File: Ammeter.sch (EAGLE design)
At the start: 81 parts, among them IC1 TL081P, IC2 TL081P, IC3 ICL7107, IC4 TL081P, IC5 TL081P, IC6 TL081P, IC7 TL081P, IC8 TL081P, IC9 TL081P, T1 BD139

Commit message: fixed errors in schematic and added BOM
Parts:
- added D4: BZX85C5V6, diode:BZX85
- added R55: 500, rcl:POTENTIOMETER_PT_SPIN
- D1, D2: value BZV10 -> BZX85C5V1; device diode:BZV10 -> diode:BZX85
- D3: value BZV10 -> BAT42; device diode:BZV10 -> diode:BAT42; SPICEPREFIX D -> (none)
- R14: value 82k -> 270
- R15: value 20k -> 270
- R17: value 270 -> 100k; device resistor:R-EU_0204/7 -> rcl:POTENTIOMETER_PT_SPIN
- R18: value 270 -> 20k
- R19: value 1M -> 100k
- R2: value 43k -> 270
- R20: value 100k -> 470k
- R21: value 470k -> 270
- R23, R9: value 270 -> 1M
- R29: value 110 -> 270
- R3: value 4k7 -> 100
- R31: value 270 -> 110
- R4: value 270 -> 50k; device resistor:R-EU_0204/7 -> rcl:POTENTIOMETER_PT_SPIN
- R46, R47: value 100k -> 15K
- R5: value 100 -> 4k7
- R50: value 16k -> 5k; device resistor:R-EU_0204/7 -> rcl:POTENTIOMETER_PT_SPIN
- R51: value (none) -> 16k; device rcl:POTENTIOMETER_PT_SPIN -> resistor:R-EU_0204/7
- R52: value 2k -> 20k; device resistor:R-EU_0204/7 -> rcl:POTENTIOMETER_PT_SPIN
- R53: value 2k -> 300
- R54: value (none) -> 2k
- R8: value 1M -> 270
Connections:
- net N$27 renamed 4-20
- removed net ICL_BP: IC3.BP, R23.1
- removed net V_REF: IC3.REF-HI
- new net N$5: DIS3.DP, R10.2
- new net N$52: IC8.OUT, R52.2
- net +12V: now also D3.C, R31.2; no longer G1.-, G2.+, R29.2
- net +5V: now also D4.C, R17.1, R31.1, R4.1; no longer D3.C, DIS1.CA1, DIS2.CA1, DIS3.CA1, R14.2, R2.2, R29.1
- net -12V: now also D3.A, G1.-, G2.+, R3.1; no longer R5.1
- net -5V: now also R3.2; no longer R5.2
- net 0-10V: no longer IC8.OUT, R51.3
- net 0.5V: now also R9.2; no longer R8.2
- net 1V: now also IC3.REF-HI, R23.2; no longer R19.2
- net GND: now also D4.A, IC3.BP, R10.1, R17.3, R18.1, R4.3, R5.1, R50.3, R51.1, R52.3, R53.2, R55.1, R55.3; no longer D3.A, R15.1, R3.1, R50.1, R51.2, R52.2, R54.1
- net ICL_A2: now also R14.1; no longer R13.1
- net ICL_B2: now also R15.1; no longer R16.1
- net ICL_B3: now also R2.1; no longer R4.1
- net ICL_C2: now also R16.1; no longer R17.1
- net ICL_D1: now also R29.1; no longer R30.1
- net ICL_D2: now also R21.1; no longer R18.1
- net ICL_E1: now also R30.1; no longer R31.1
- net ICL_E3: now also R8.1; no longer R9.1
- net ICL_F3: now also R13.1; no longer R12.1
- net ICL_G3: now also R12.1; no longer R10.1
- net ICL_IN: now also R54.2; no longer R53.2
- net N$1: now also R19.1; no longer R20.1
- net N$10: now also R20.1; no longer R21.1
- net N$11: now also R23.1; no longer R19.1
- net N$12: now also R4.2, R5.2; no longer R2.1, R3.2
- net N$13: now also R17.2, R18.2; no longer R14.1, R15.2
- net N$16: now also R52.1; no longer R51.1
- net N$18: now also R51.2; no longer R50.2
- net N$2: now also R19.2; no longer R20.2
- net N$25: now also R55.2; no longer R54.2
- net N$30: now also R29.2; no longer R30.2
- net N$31: now also R30.2; no longer R31.2
- net N$33: now also R14.2; no longer R13.2
- net N$35: now also R21.2; no longer R18.2
- net N$36: now also R15.2; no longer R16.2
- net N$37: now also R16.2; no longer R17.2
- net N$43: now also R2.2; no longer R4.2
- net N$45: now also R8.2; no longer R9.2
- net N$46: now also R13.2; no longer R12.2
- net N$47: now also R12.2; no longer R10.2
- net N$48: now also R46.2, R50.2; no longer DIS2.DP, R23.2
- net N$49: now also R50.1, R53.1; no longer R46.2, R52.1
- net N$51: now also R54.1; no longer R53.1
- net N$7: now also R9.1; no longer R8.1
- net N$9: now also R20.2; no longer R21.2
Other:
- moved on the sheet: C8, DIS2, G1, G2, IC1, IC2, IC9, R13, R14, R15, R16, R18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

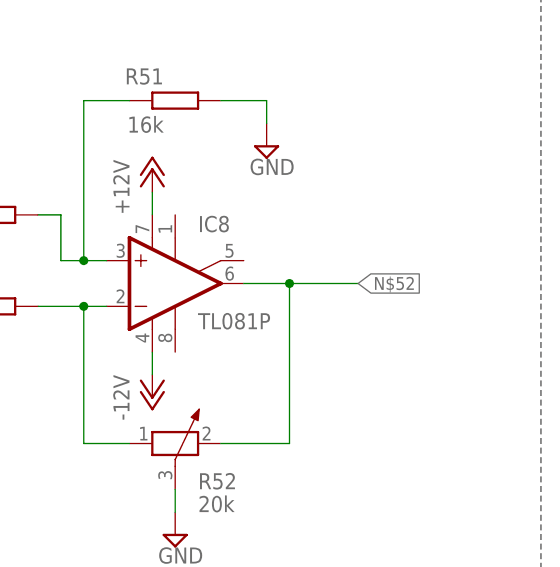
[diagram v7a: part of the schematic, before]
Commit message: hotfix (incorrect label in schematic)
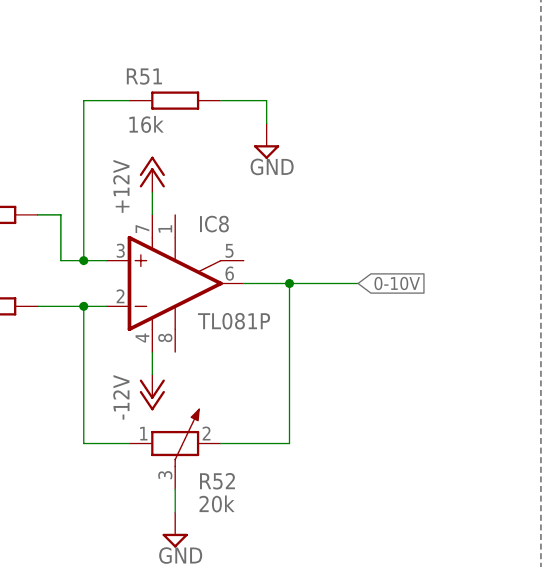
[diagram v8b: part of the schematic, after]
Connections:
- removed net N$52: IC8.OUT, R52.2
- net 0-10V: now also IC8.OUT, R52.2
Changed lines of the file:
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@@
 <setting verticaltext="up"/>
 </settings>
-<grid distance="0.1" unitdist="inch" unit="inch" style="lines" multiple="1" display="yes" altdistance="0.01" altunitdist="inch" altunit="inch"/>
+<grid distance="0.1" unitdist="inch" unit="inch" style="lines" multiple="1" display="no" altdistance="0.01" altunitdist="inch" altunit="inch"/>
 <layers>
 <layer number="1" name="Top" color="4" fill="1" visible="no" active="no"/>
@@
 <pinref part="R34" gate="G$1" pin="2"/>
 </segment>
+<segment>
+<pinref part="IC8" gate="A" pin="OUT"/>
+<wire x1="287.02" y1="157.48" x2="279.4" y2="157.48" width="0.1524" layer="91"/>
+<label x="287.02" y="157.48" size="1.4224" layer="95" xref="yes"/>
+<pinref part="R52" gate="1" pin="2"/>
+<wire x1="279.4" y1="157.48" x2="274.32" y2="157.48" width="0.1524" layer="91"/>
+<wire x1="271.78" y1="139.7" x2="279.4" y2="139.7" width="0.1524" layer="91"/>
+<wire x1="279.4" y1="139.7" x2="279.4" y2="157.48" width="0.1524" layer="91"/>
+<junction x="279.4" y="157.48"/>
+</segment>
 </net>
 <net name="N$17" class="0">
@@
 </segment>
 </net>
-<net name="N$52" class="0">
-<segment>
-<pinref part="IC8" gate="A" pin="OUT"/>
-<wire x1="287.02" y1="157.48" x2="279.4" y2="157.48" width="0.1524" layer="91"/>
-<label x="287.02" y="157.48" size="1.4224" layer="95" xref="yes"/>
-<pinref part="R52" gate="1" pin="2"/>
-<wire x1="279.4" y1="157.48" x2="274.32" y2="157.48" width="0.1524" layer="91"/>
-<wire x1="271.78" y1="139.7" x2="279.4" y2="139.7" width="0.1524" layer="91"/>
-<wire x1="279.4" y1="139.7" x2="279.4" y2="157.48" width="0.1524" layer="91"/>
-<junction x="279.4" y="157.48"/>
-</segment>
-</net>
